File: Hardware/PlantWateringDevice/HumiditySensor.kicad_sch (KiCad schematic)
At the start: 12 parts, among them J1 Conn_01x03_Pin, U1 MCP6002-xSN

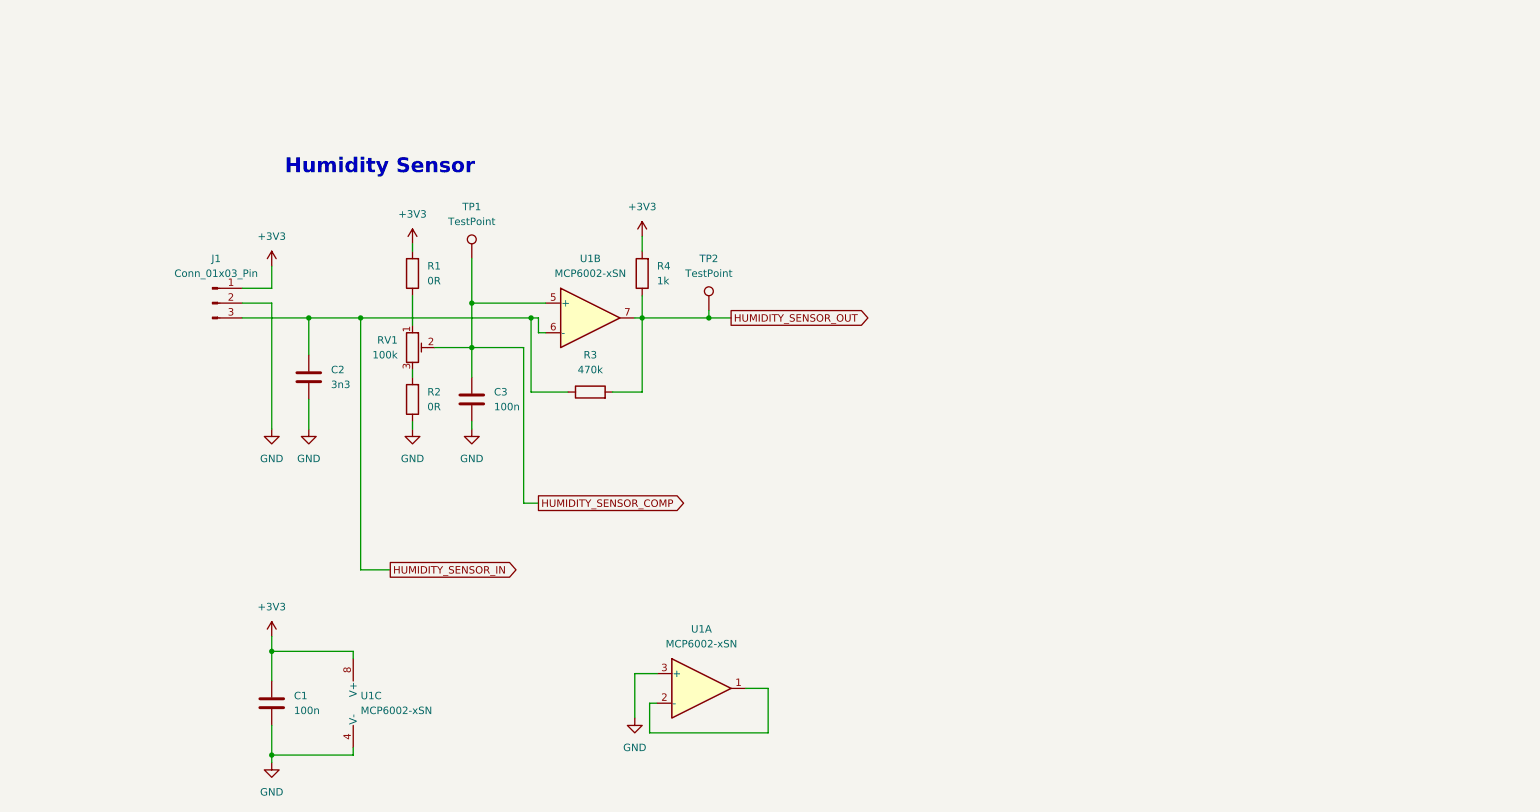
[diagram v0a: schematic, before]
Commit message: circuit simplification
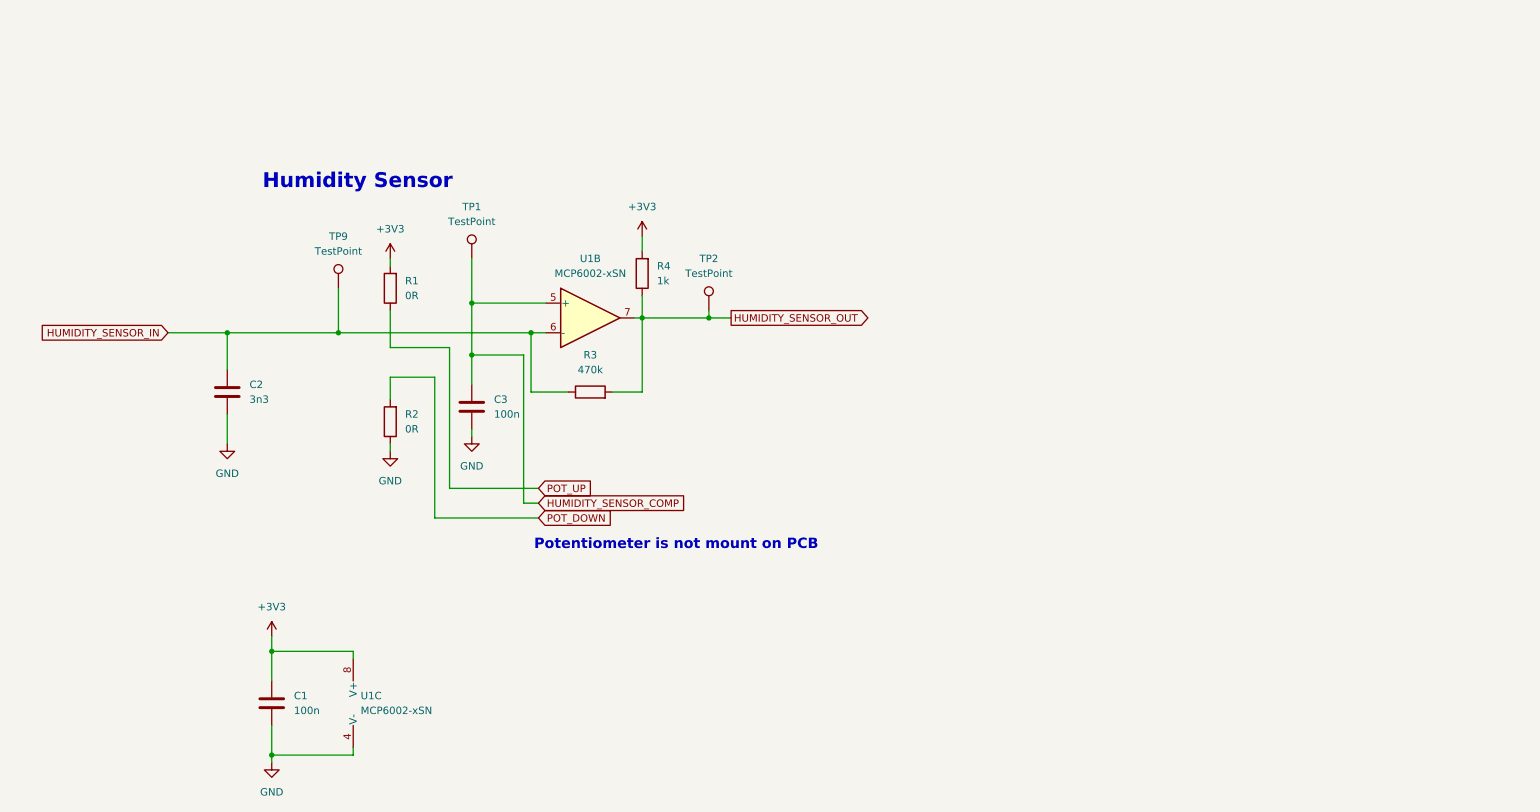
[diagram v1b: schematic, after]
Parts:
- removed J1: Conn_01x03_Pin, Connector_PinHeader_2.54mm:PinHeader_1x03_P2.54mm_Horizontal, symbol Connector:Conn_01x03_Pin
- removed RV1: 100k, Connector_PinHeader_2.54mm:PinHeader_1x03_P2.54mm_Vertical, symbol Device:R_Potentiometer_Trim
- removed unit 1 of U1
- added TP9: TestPoint, TestPoint:TestPoint_Pad_D1.5mm, symbol Connector:TestPoint
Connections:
- net HUMIDITY_SENSOR_IN: now also TP9.1
- net POT_UP: now reaches R1.1
- net POT_DOWN: now reaches R2.2
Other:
- note added: "Potentiometer is not mount on PCB"
- moved on the sheet: C2, C3, R1, R2

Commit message: improvements after eric's comments
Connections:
- net +3V3 renamed VCC

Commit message: firmware implementation
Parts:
- R3: now not fitted; now left out of the parts list
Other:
- note added: "LED TO TP2 pzelaczniki foopriny"
- note added: "POSITIVE FEEDBACK"
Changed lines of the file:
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@@
 	(generator_version "9.0")
 	(paper "A4")
+	(text "LED TO TP2 pzelaczniki foopriny"
+		(exclude_from_sim no)
+		(at 201.676 20.32 0)
+		(effects
+			(font
+				(size 5.08 5.08)
+				(thickness 1.27)
+				(bold yes)
+			)
+		)
+	)
+	(text "POSITIVE FEEDBACK"
+		(exclude_from_sim no)
+		(at 153.416 132.842 0)
+		(effects
+			(font
+				(size 5.08 5.08)
+				(thickness 1.27)
+				(bold yes)
+			)
+		)
+	)
 	(text "Potentiometer is not mount on PCB"
 		(exclude_from_sim no)
@@
 		(at 118.11 80.01 90)
 		(unit 1)
-		(exclude_from_sim no)
-		(in_bom yes)
-		(on_board yes)
-		(dnp no)
+		(exclude_from_sim yes)
+		(in_bom no)
+		(on_board no)
+		(dnp yes)
 		(fields_autoplaced yes)
 		(property "Reference" "R3"

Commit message: fix #29, fix #31
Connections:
- net HUMIDITY_SENSOR_COMP renamed POTENTIOMETER_DATA
- net HUMIDITY_SENSOR_IN renamed HUMIDITY_SENSOR
- net HUMIDITY_SENSOR_OUT renamed HUMIDITY_COMPARATION
- net POT_DOWN renamed POTENTIOMETER_VSS
- net POT_UP renamed POTENTIOMETER_VCC
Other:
- note removed: "LED TO TP2 pzelaczniki foopriny"
- note removed: "POSITIVE FEEDBACK"
- moved on the sheet: R4, TP2
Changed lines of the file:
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@@
 	(generator_version "9.0")
 	(paper "A4")
-	(text "LED TO TP2 pzelaczniki foopriny"
-		(exclude_from_sim no)
-		(at 201.676 20.32 0)
-		(effects
-			(font
-				(size 5.08 5.08)
-				(thickness 1.27)
-				(bold yes)
-			)
-		)
-	)
-	(text "POSITIVE FEEDBACK"
-		(exclude_from_sim no)
-		(at 153.416 132.842 0)
-		(effects
-			(font
-				(size 5.08 5.08)
-				(thickness 1.27)
-				(bold yes)
-			)
-		)
-	)
 	(text "Potentiometer is not mount on PCB"
 		(exclude_from_sim no)
-		(at 132.842 106.172 0)
+		(at 116.586 109.22 0)
 		(effects
 			(font
@@
 	)
 	(junction
+		(at 134.62 67.31)
+		(diameter 0)
+		(color 0 0 0 0)
+	)
+	(junction
 		(at 55.88 69.85)
 		(diameter 0)
@@
 	)
 	(junction
-		(at 138.43 67.31)
+		(at 146.05 67.31)
 		(diameter 0)
 		(color 0 0 0 0)
@@
 	(wire
 		(pts
-			(xy 127 67.31) (xy 138.43 67.31)
-		)
-		(stroke
-			(width 0)
-			(type default)
-		)
-	)
-	(wire
-		(pts
 			(xy 97.79 73.66) (xy 97.79 78.74)
 		)
@@
 	(wire
 		(pts
-			(xy 138.43 67.31) (xy 142.24 67.31)
+			(xy 146.05 67.31) (xy 149.86 67.31)
 		)
 		(stroke
@@
 	(wire
 		(pts
-			(xy 127 63.5) (xy 127 67.31)
-		)
-		(stroke
-			(width 0)
-			(type default)
-		)
-	)
-	(wire
-		(pts
-			(xy 138.43 66.04) (xy 138.43 67.31)
+			(xy 134.62 63.5) (xy 134.62 67.31)
+		)
+		(stroke
+			(width 0)
+			(type default)
+		)
+	)
+	(wire
+		(pts
+			(xy 146.05 66.04) (xy 146.05 67.31)
 		)
 		(stroke
@@
 	(wire
 		(pts
+			(xy 127 67.31) (xy 134.62 67.31)
+		)
+		(stroke
+			(width 0)
+			(type default)
+		)
+	)
+	(wire
+		(pts
 			(xy 109.22 96.52) (xy 93.98 96.52)
 		)
@@
 	(wire
 		(pts
+			(xy 134.62 67.31) (xy 146.05 67.31)
+		)
+		(stroke
+			(width 0)
+			(type default)
+		)
+	)
+	(wire
+		(pts
 			(xy 106.68 99.06) (xy 109.22 99.06)
 		)
@@
 	(wire
 		(pts
-			(xy 127 53.34) (xy 127 55.88)
+			(xy 134.62 53.34) (xy 134.62 55.88)
 		)
 		(stroke
@@
 		)
 	)
-	(global_label "HUMIDITY_SENSOR_COMP"
+	(global_label "POTENTIOMETER_DATA"
 		(shape input)
 		(at 109.22 99.06 0)
@@
 		)
 		(property "Intersheetrefs" "${INTERSHEET_REFS}"
-			(at 135.6095 99.06 0)
+			(at 132.5251 99.06 0)
 			(effects
 				(font
@@
 		)
 	)
-	(global_label "HUMIDITY_SENSOR_OUT"
+	(global_label "HUMIDITY_COMPARATION"
 		(shape output)
-		(at 142.24 67.31 0)
+		(at 149.86 67.31 0)
 		(fields_autoplaced yes)
 		(effects
@@
 		)
 		(property "Intersheetrefs" "${INTERSHEET_REFS}"
-			(at 166.9362 67.31 0)
+			(at 175.4635 67.31 0)
 			(effects
 				(font
@@
 		)
 	)
-	(global_label "POT_UP"
+	(global_label "POTENTIOMETER_VCC"
 		(shape input)
 		(at 109.22 96.52 0)
@@
 		)
 		(property "Intersheetrefs" "${INTERSHEET_REFS}"
-			(at 119.3414 96.52 0)
+			(at 131.7389 96.52 0)
 			(effects
 				(font
@@
 		)
 	)
-	(global_label "POT_DOWN"
+	(global_label "POTENTIOMETER_VSS"
 		(shape input)
 		(at 109.22 101.6 0)
@@
 		)
 		(property "Intersheetrefs" "${INTERSHEET_REFS}"
-			(at 122.1233 101.6 0)
+			(at 131.6179 101.6 0)
 			(effects
 				(font
@@
 		)
 	)
-	(global_label "HUMIDITY_SENSOR_IN"
+	(global_label "HUMIDITY_SENSOR"
 		(shape input)
 		(at 45.72 69.85 180)
@@
 		)
 		(property "Intersheetrefs" "${INTERSHEET_REFS}"
-			(at 22.7171 69.85 0)
+			(at 25.62 69.85 0)
 			(effects
 				(font
@@
 	(symbol
 		(lib_id "Device:R")
-		(at 127 59.69 180)
+		(at 134.62 59.69 180)
 		(unit 1)
 		(exclude_from_sim no)
@@
 		(fields_autoplaced yes)
 		(property "Reference" "R4"
-			(at 129.54 58.4199 0)
+			(at 137.16 58.4199 0)
 			(effects
 				(font
@@
 		)
 		(property "Value" "1k"
-			(at 129.54 60.9599 0)
+			(at 137.16 60.9599 0)
 			(effects
 				(font
@@
 		)
 		(property "Footprint" "Resistor_SMD:R_0805_2012Metric"
-			(at 128.778 59.69 90)
+			(at 136.398 59.69 90)
 			(effects
 				(font
@@
 		)
 		(property "Datasheet" "~"
-			(at 127 59.69 0)
+			(at 134.62 59.69 0)
 			(effects
 				(font
@@
 		)
 		(property "Description" "Resistor"
-			(at 127 59.69 0)
+			(at 134.62 59.69 0)
 			(effects
 				(font
@@
 	(symbol
 		(lib_id "Connector:TestPoint")
-		(at 138.43 66.04 0)
+		(at 146.05 66.04 0)
 		(unit 1)
 		(exclude_from_sim no)
@@
 		(fields_autoplaced yes)
 		(property "Reference" "TP2"
-			(at 138.43 57.15 0)
+			(at 146.05 57.15 0)
 			(effects
 				(font
@@
 		)
 		(property "Value" "TestPoint"
-			(at 138.43 59.69 0)
+			(at 146.05 59.69 0)
 			(effects
 				(font
@@
 		)
 		(property "Footprint" "TestPoint:TestPoint_Pad_D1.5mm"
-			(at 143.51 66.04 0)
+			(at 151.13 66.04 0)
 			(effects
 				(font
@@
 		)
 		(property "Datasheet" "~"
-			(at 143.51 66.04 0)
+			(at 151.13 66.04 0)
 			(effects
 				(font
@@
 		)
 		(property "Description" "test point"
-			(at 138.43 66.04 0)
+			(at 146.05 66.04 0)
 			(effects
 				(font
@@
 	(symbol
 		(lib_id "power:VCC")
-		(at 127 53.34 0)
+		(at 134.62 53.34 0)
 		(unit 1)
 		(exclude_from_sim no)
@@
 		(fields_autoplaced yes)
 		(property "Reference" "#PWR025"
-			(at 127 57.15 0)
+			(at 134.62 57.15 0)
 			(effects
 				(font
@@
 		)
 		(property "Value" "VCC"
-			(at 127 48.26 0)
+			(at 134.62 48.26 0)
 			(effects
 				(font
@@
 		)
 		(property "Footprint" ""
-			(at 127 53.34 0)
+			(at 134.62 53.34 0)
 			(effects
 				(font
@@
 		)
 		(property "Datasheet" ""
-			(at 127 53.34 0)
+			(at 134.62 53.34 0)
 			(effects
 				(font
@@
 		)
 		(property "Description" "Power symbol creates a global label with name \"VCC\""
-			(at 127 53.34 0)
-			(effects
-				(font
+			(at 134.62 53.34 0)
+			(effects
+				(font

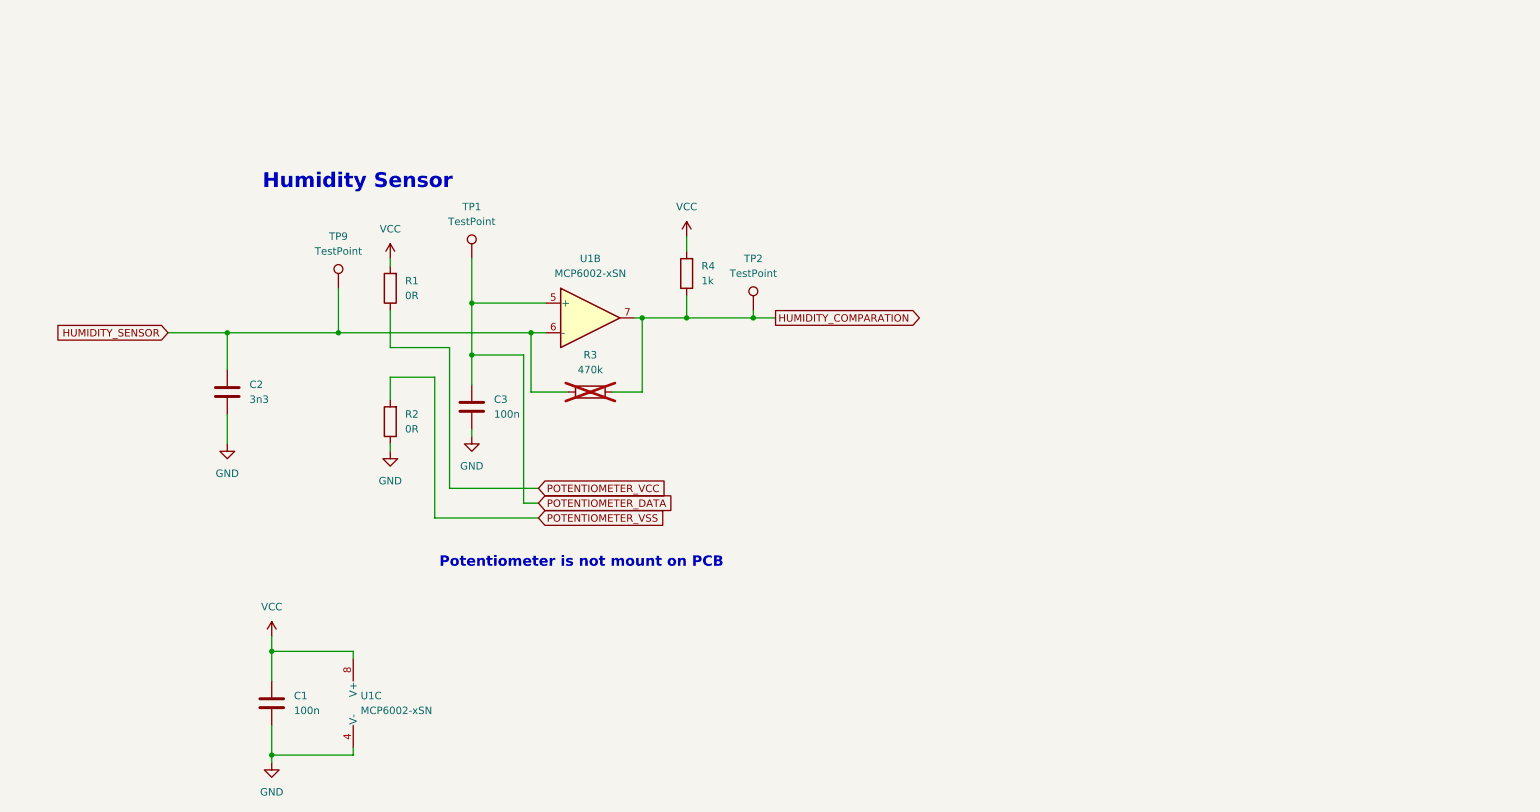
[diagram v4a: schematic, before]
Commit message: fix #16, fix #17, fix #18, fix #19, fix #20, fix #26, fix #27, fix #28, fix #30, fix #32, fix#33, fix #34, fix #35, fix #38
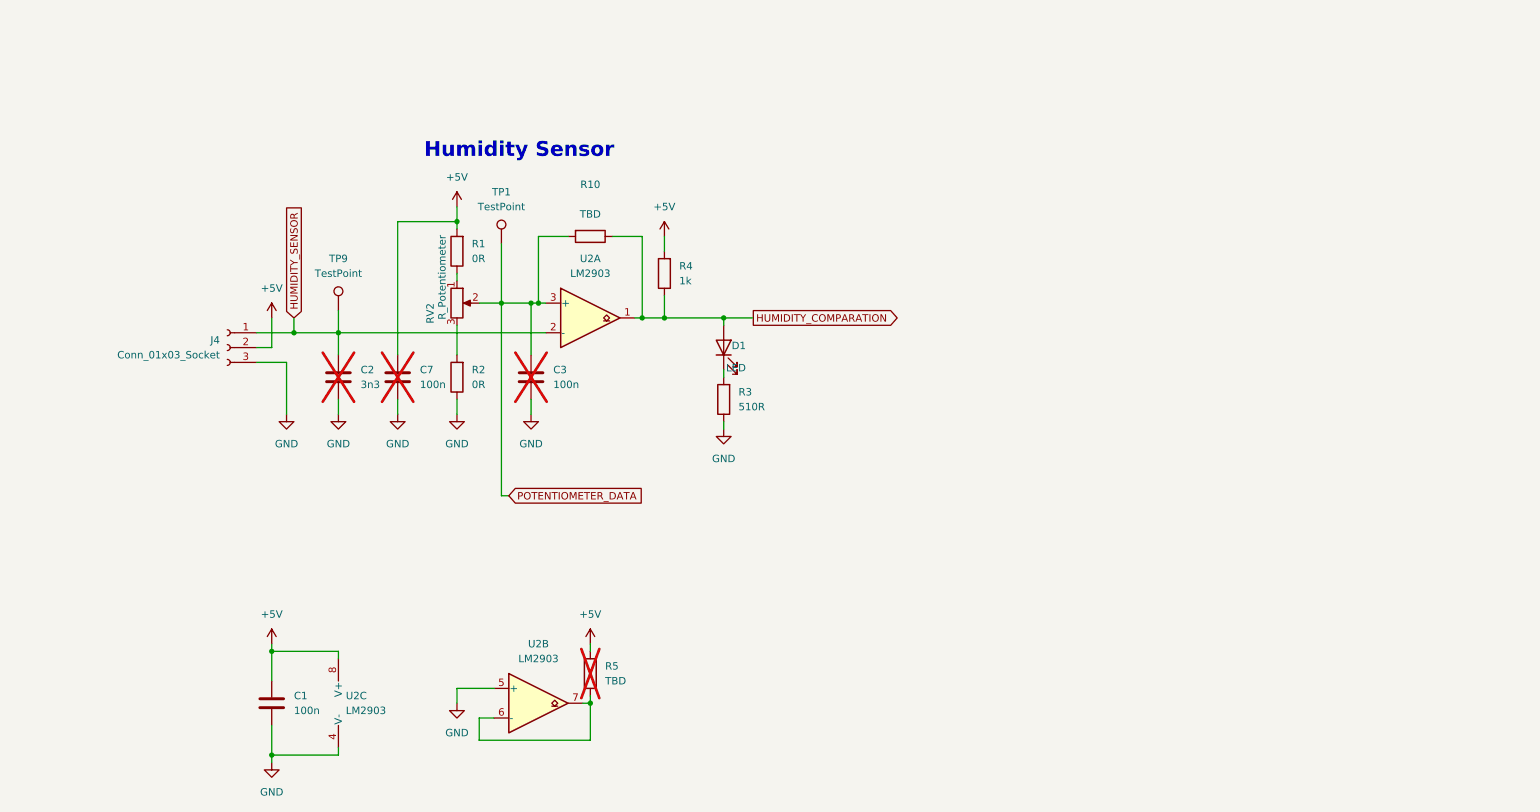
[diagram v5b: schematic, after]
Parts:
- removed TP2: TestPoint, TestPoint:TestPoint_Pad_D1.5mm, symbol Connector:TestPoint
- removed U1: MCP6002-xSN, Package_SO:SO-8_3.9x4.9mm_P1.27mm, symbol Amplifier_Operational:MCP6002-xSN
- added C7: 100n, Capacitor_SMD:C_0603_1608Metric, symbol Device:C
- added D1: LED, LED_THT:LED_D4.0mm, symbol Device:LED
- added J4: Conn_01x03_Socket, Connector_JST:JST_EH_B3B-EH-A_1x03_P2.50mm_Vertical, symbol Connector:Conn_01x03_Socket
- added R10, R5: TBD, Resistor_SMD:R_0603_1608Metric, symbol Device:R
- added RV2: R_Potentiometer, Potentiometer_THT:Potentiometer_Alps_RK09L_Single_Vertical, symbol Device:R_Potentiometer
- added U2: LM2903, Package_SO:TSSOP-8_3x3mm_P0.65mm, symbol Comparator:LM2903
- C1: footprint Capacitor_SMD:C_0805_2012Metric -> Capacitor_SMD:C_0603_1608Metric
- C2, C3: footprint Capacitor_SMD:C_0805_2012Metric -> Capacitor_SMD:C_0603_1608Metric; now not fitted; now left out of the parts list
- R1, R2, R4: footprint Resistor_SMD:R_0805_2012Metric -> Resistor_SMD:R_0603_1608Metric
- R3: value 470k -> 510R; footprint Resistor_SMD:R_0805_2012Metric -> Resistor_SMD:R_0603_1608Metric; now fitted; now in the parts list
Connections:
- net GND: now also R3.1, C7.2, J4.3 (Pin_3), U2.4 (V-), U2.5 (+)
- net HUMIDITY_COMPARATION: now also D1.2 (A), R10.1, U2.1; no longer R3.2
- net HUMIDITY_SENSOR: now also J4.1 (Pin_1), U2.2 (-); no longer R3.1
- net POTENTIOMETER_DATA: now also R10.2, RV2.2, U2.3 (+)
- net POTENTIOMETER_VCC: no longer names the net of R1.1
- net POTENTIOMETER_VCC: now also RV2.1
- net POTENTIOMETER_VSS: no longer names the net of R2.2
- net POTENTIOMETER_VSS: now also RV2.3
- net VCC renamed +5V
- net +5V: now also C7.1, J4.2 (Pin_2), R5.2, U2.8 (V+)
- new net: D1.1 (K), R3.2
- new net: R5.1, U2.6 (-), U2.7
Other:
- note removed: "Potentiometer is not mount on PCB"
- moved on the sheet: R1, R2, R4, TP1, TP9
